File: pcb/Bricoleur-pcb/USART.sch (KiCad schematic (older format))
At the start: 1 part, among them J3 Conn_02x03_Odd_Even

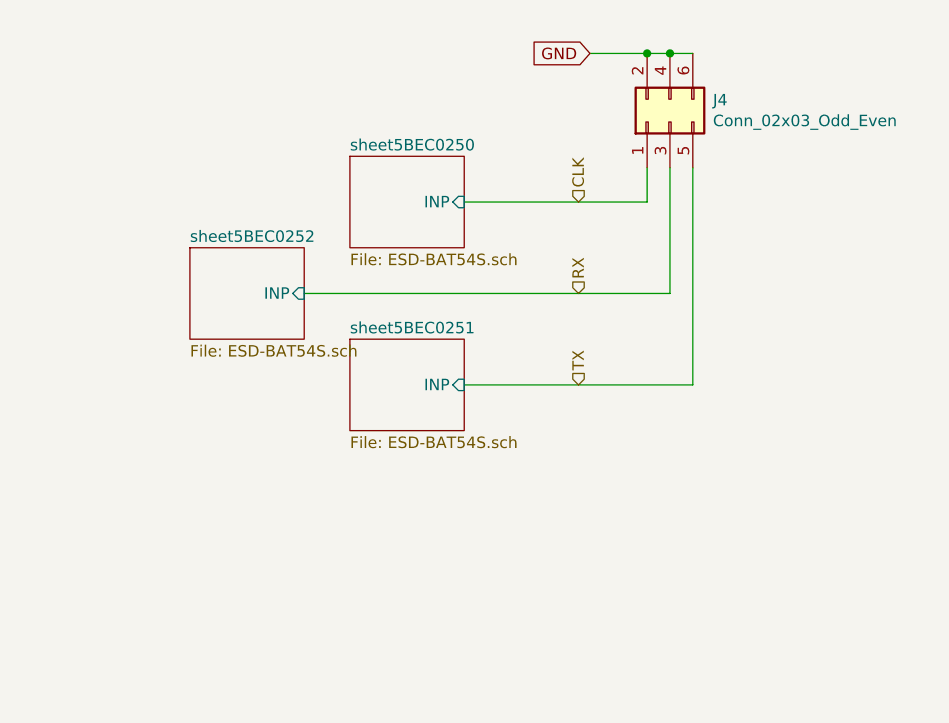
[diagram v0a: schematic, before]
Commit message: Narrowed down component placement, continued routing
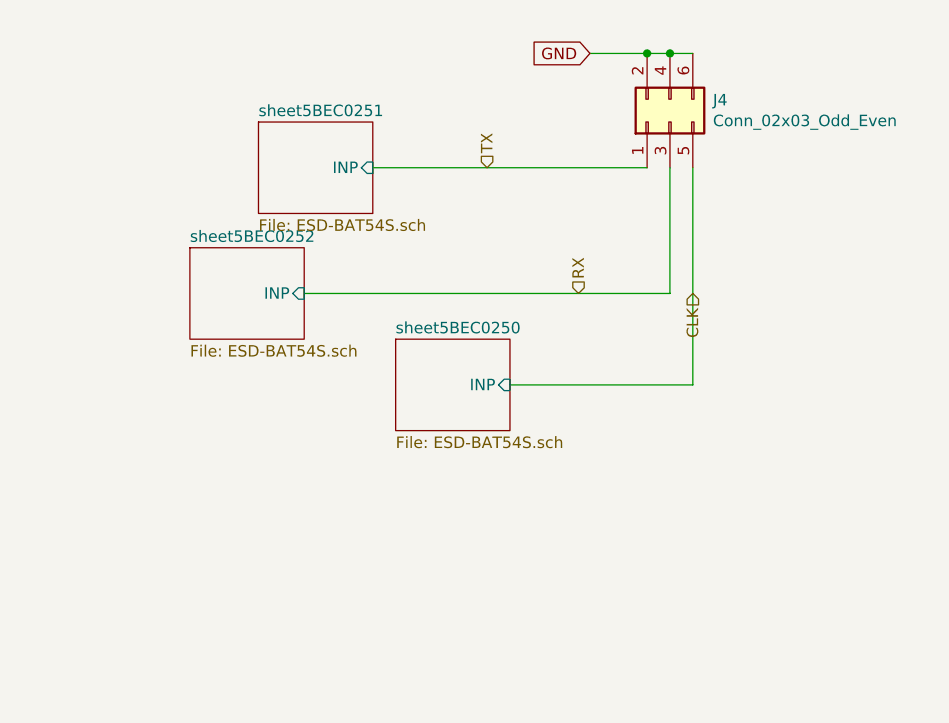
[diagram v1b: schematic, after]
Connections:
- net CLK: now also J3.5 (Pin_5); no longer J3.1 (Pin_1)
- net TX: now also J3.1 (Pin_1); no longer J3.5 (Pin_5)
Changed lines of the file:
@@
 $Descr A4 11693 8268
 encoding utf-8
-Sheet 11 18
+Sheet 15 18
 Title ""
 Date ""
@@
 $EndDescr
 $Sheet
-S 2300 2500 500  400
+S 2500 3300 500  400
 U 5BEC0255
 F0 "sheet5BEC0250" 50
 F1 "ESD-BAT54S.sch" 50
-F2 "INP" I R 2800 2700 50
+F2 "INP" I R 3000 3500 50
 $EndSheet
 $Sheet
-S 2300 3300 500  400
+S 1900 2350 500  400
 U 5BEC0258
 F0 "sheet5BEC0251" 50
 F1 "ESD-BAT54S.sch" 50
-F2 "INP" I R 2800 3500 50
+F2 "INP" I R 2400 2550 50
 $EndSheet
 $Sheet
@@
 $EndComp
 Wire Wire Line
-	3600 2550 3600 2700
-Wire Wire Line
-	2800 2700 3600 2700
+	3000 3500 3800 3500
 Wire Wire Line
 	3700 2550 3700 3100
@@
 Wire Wire Line
 	3800 2550 3800 3500
-Wire Wire Line
-	2800 3500 3800 3500
 Text GLabel 3350 2050 0    50   Input ~ 0
 GND
@@
 	3700 2050 3800 2050
 Connection ~ 3700 2050
-Text HLabel 3300 2700 1    50   Input ~ 0
+Text HLabel 3800 3100 3    50   Input ~ 0
 CLK
 Text HLabel 3300 3100 1    50   Input ~ 0
 RX
-Text HLabel 3300 3500 1    50   Input ~ 0
+Text HLabel 2900 2550 1    50   Input ~ 0
 TX
+Wire Wire Line
+	2400 2550 3600 2550
 $EndSCHEMATC

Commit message: Moar routing
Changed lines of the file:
@@
 $Descr A4 11693 8268
 encoding utf-8
-Sheet 15 18
+Sheet 11 18
 Title ""
 Date ""
@@
 AR Path="/5BEB800B/5BEC0490" Ref="J3"  Part="1"
 AR Path="/5BEE7FFD/5BEC0490" Ref="J4"  Part="1"
-F 0 "J4" V 3796 2162 50  0000 R CNN
+F 0 "J3" V 3796 2162 50  0000 R CNN
 F 1 "Conn_02x03_Odd_Even" V 3705 2162 50  0000 R CNN
 F 2 "Connector_IDC:IDC-Header_2x03_P2.54mm_Vertical" H 3700 2350 50  0001 C CNN

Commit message: Big fookup.
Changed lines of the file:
@@
 $Descr A4 11693 8268
 encoding utf-8
-Sheet 11 18
+Sheet 15 18
 Title ""
 Date ""
@@
 AR Path="/5BEB800B/5BEC0490" Ref="J3"  Part="1"
 AR Path="/5BEE7FFD/5BEC0490" Ref="J4"  Part="1"
-F 0 "J3" V 3796 2162 50  0000 R CNN
+F 0 "J4" V 3796 2162 50  0000 R CNN
 F 1 "Conn_02x03_Odd_Even" V 3705 2162 50  0000 R CNN
 F 2 "Connector_IDC:IDC-Header_2x03_P2.54mm_Vertical" H 3700 2350 50  0001 C CNN

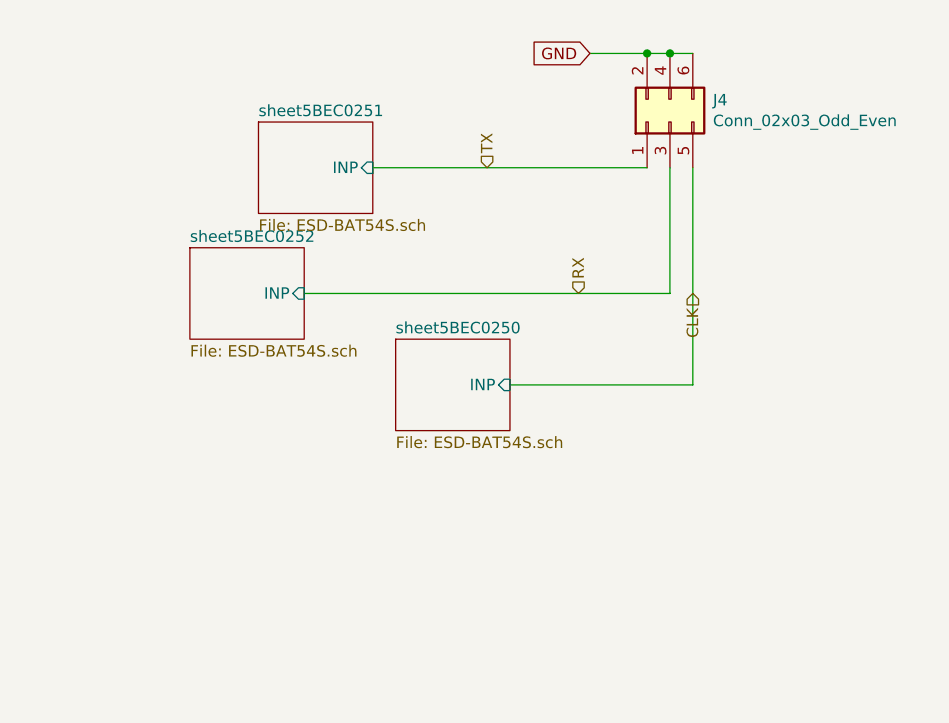
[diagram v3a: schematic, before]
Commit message: Cleanup, labeling, schematic size reduction
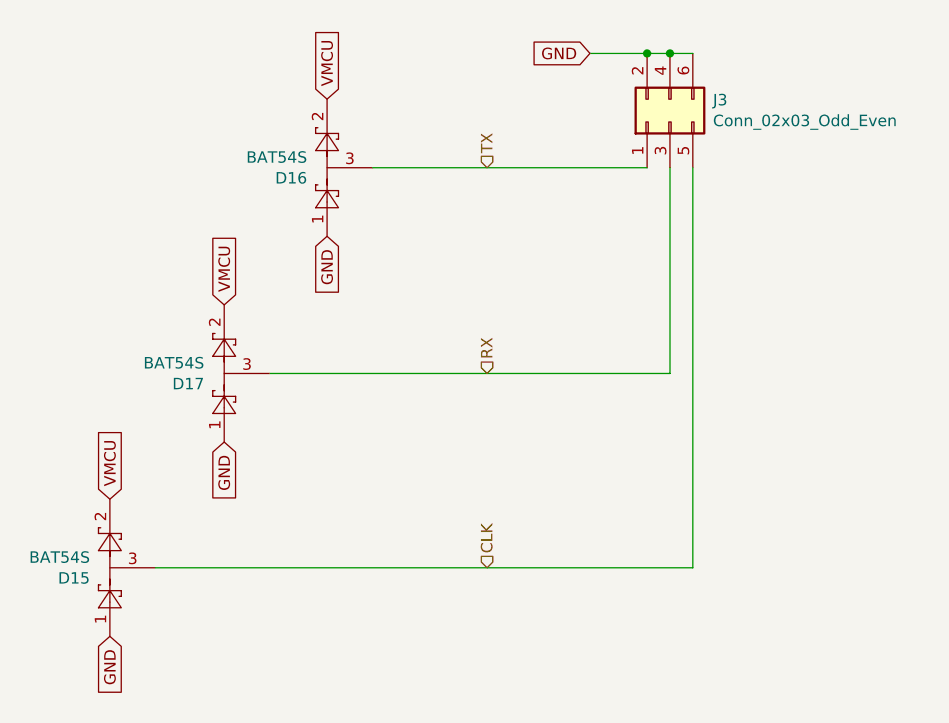
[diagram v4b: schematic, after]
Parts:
- added D17, D18, D19: BAT54S, Package_TO_SOT_SMD:SOT-23, symbol Diode:BAT54S
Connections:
- net CLK: now also D18.3
- net GND: now also D17.1, D18.1, D19.1
- net RX: now also D17.3
- net TX: now also D19.3
- new net VMCU: D17.2, D18.2, D19.2
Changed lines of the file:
@@
 $Descr A4 11693 8268
 encoding utf-8
-Sheet 15 18
+Sheet 4 5
 Title ""
 Date ""
@@
 Comment4 ""
 $EndDescr
-$Sheet
-S 2500 3300 500  400
-U 5BEC0255
-F0 "sheet5BEC0250" 50
-F1 "ESD-BAT54S.sch" 50
-F2 "INP" I R 3000 3500 50
-$EndSheet
-$Sheet
-S 1900 2350 500  400
-U 5BEC0258
-F0 "sheet5BEC0251" 50
-F1 "ESD-BAT54S.sch" 50
-F2 "INP" I R 2400 2550 50
-$EndSheet
-$Sheet
-S 1600 2900 500  400
-U 5BEC025B
-F0 "sheet5BEC0252" 50
-F1 "ESD-BAT54S.sch" 50
-F2 "INP" I R 2100 3100 50
-$EndSheet
 $Comp
 L Connector_Generic:Conn_02x03_Odd_Even J3
@@
 AR Path="/5BEB800B/5BEC0490" Ref="J3"  Part="1"
 AR Path="/5BEE7FFD/5BEC0490" Ref="J4"  Part="1"
-F 0 "J4" V 3796 2162 50  0000 R CNN
+F 0 "J3" V 3796 2162 50  0000 R CNN
 F 1 "Conn_02x03_Odd_Even" V 3705 2162 50  0000 R CNN
 F 2 "Connector_IDC:IDC-Header_2x03_P2.54mm_Vertical" H 3700 2350 50  0001 C CNN
@@
 $EndComp
 Wire Wire Line
-	3000 3500 3800 3500
+	1450 4300 3800 4300
 Wire Wire Line
-	3700 2550 3700 3100
+	3700 2550 3700 3450
 Wire Wire Line
-	2100 3100 3700 3100
+	1950 3450 3700 3450
 Wire Wire Line
-	3800 2550 3800 3500
+	3800 2550 3800 4300
 Text GLabel 3350 2050 0    50   Input ~ 0
 GND
@@
 	3700 2050 3800 2050
 Connection ~ 3700 2050
-Text HLabel 3800 3100 3    50   Input ~ 0
+Text HLabel 2900 4300 1    50   Input ~ 0
 CLK
-Text HLabel 3300 3100 1    50   Input ~ 0
+Text HLabel 2900 3450 1    50   Input ~ 0
 RX
 Text HLabel 2900 2550 1    50   Input ~ 0
@@
 Wire Wire Line
 	2400 2550 3600 2550
+$Comp
+L Diode:BAT54S D?
+U 1 1 5BFCE38E
+P 1250 4300
+AR Path="/5BB71F0F/5BFCE38E" Ref="D?"  Part="1"
+AR Path="/5BB7B6EA/5BFCE38E" Ref="D?"  Part="1"
+AR Path="/5BCBFDFB/5BFCE38E" Ref="D?"  Part="1"
+AR Path="/5BDAE386/5BDAE7CD/5BFCE38E" Ref="D?"  Part="1"
+AR Path="/5BDAE386/5BDAE90A/5BFCE38E" Ref="D?"  Part="1"
+AR Path="/5BDAE386/5BDAE977/5BFCE38E" Ref="D?"  Part="1"
+AR Path="/5BDAE386/5BDAEF7E/5BFCE38E" Ref="D?"  Part="1"
+AR Path="/5BEB800B/5BEC0255/5BFCE38E" Ref="D?"  Part="1"
+AR Path="/5BEB800B/5BEC0258/5BFCE38E" Ref="D?"  Part="1"
+AR Path="/5BEB800B/5BEC025B/5BFCE38E" Ref="D?"  Part="1"
+AR Path="/5BEE7FFD/5BEC0255/5BFCE38E" Ref="D?"  Part="1"
+AR Path="/5BEE7FFD/5BEC0258/5BFCE38E" Ref="D?"  Part="1"
+AR Path="/5BEE7FFD/5BEC025B/5BFCE38E" Ref="D?"  Part="1"
+AR Path="/5BEE7FFD/5BFCE38E" Ref="D18"  Part="1"
+AR Path="/5BEB800B/5BFCE38E" Ref="D15"  Part="1"
+F 0 "D15" V 1204 4387 50  0000 L CNN
+F 1 "BAT54S" V 1295 4387 50  0000 L CNN
+F 2 "Package_TO_SOT_SMD:SOT-23" H 1325 4425 50  0001 L CNN
+F 3 "https://www.diodes.com/assets/Datasheets/ds11005.pdf" H 1130 4300 50  0001 C CNN
+	1    1250 4300
+	0    -1   -1   0
+$EndComp
+Text GLabel 1250 4600 3    50   Input ~ 0
+GND
+Text GLabel 1250 4000 1    50   Input ~ 0
+VMCU
+$Comp
+L Diode:BAT54S D?
+U 1 1 5BFCE61A
+P 1750 3450
+AR Path="/5BB71F0F/5BFCE61A" Ref="D?"  Part="1"
+AR Path="/5BB7B6EA/5BFCE61A" Ref="D?"  Part="1"
+AR Path="/5BCBFDFB/5BFCE61A" Ref="D?"  Part="1"
+AR Path="/5BDAE386/5BDAE7CD/5BFCE61A" Ref="D?"  Part="1"
+AR Path="/5BDAE386/5BDAE90A/5BFCE61A" Ref="D?"  Part="1"
+AR Path="/5BDAE386/5BDAE977/5BFCE61A" Ref="D?"  Part="1"
+AR Path="/5BDAE386/5BDAEF7E/5BFCE61A" Ref="D?"  Part="1"
+AR Path="/5BEB800B/5BEC0255/5BFCE61A" Ref="D?"  Part="1"
+AR Path="/5BEB800B/5BEC0258/5BFCE61A" Ref="D?"  Part="1"
+AR Path="/5BEB800B/5BEC025B/5BFCE61A" Ref="D?"  Part="1"
+AR Path="/5BEE7FFD/5BEC0255/5BFCE61A" Ref="D?"  Part="1"
+AR Path="/5BEE7FFD/5BEC0258/5BFCE61A" Ref="D?"  Part="1"
+AR Path="/5BEE7FFD/5BEC025B/5BFCE61A" Ref="D?"  Part="1"
+AR Path="/5BEB800B/5BFCE61A" Ref="D17"  Part="1"
+AR Path="/5BEE7FFD/5BFCE61A" Ref="D20"  Part="1"
+F 0 "D17" V 1704 3537 50  0000 L CNN
+F 1 "BAT54S" V 1795 3537 50  0000 L CNN
+F 2 "Package_TO_SOT_SMD:SOT-23" H 1825 3575 50  0001 L CNN
+F 3 "https://www.diodes.com/assets/Datasheets/ds11005.pdf" H 1630 3450 50  0001 C CNN
+	1    1750 3450
+	0    -1   -1   0
+$EndComp
+Text GLabel 1750 3750 3    50   Input ~ 0
+GND
+Text GLabel 1750 3150 1    50   Input ~ 0
+VMCU
+$Comp
+L Diode:BAT54S D?
+U 1 1 5BFCE778
+P 2200 2550
+AR Path="/5BB71F0F/5BFCE778" Ref="D?"  Part="1"
+AR Path="/5BB7B6EA/5BFCE778" Ref="D?"  Part="1"
+AR Path="/5BCBFDFB/5BFCE778" Ref="D?"  Part="1"
+AR Path="/5BDAE386/5BDAE7CD/5BFCE778" Ref="D?"  Part="1"
+AR Path="/5BDAE386/5BDAE90A/5BFCE778" Ref="D?"  Part="1"
+AR Path="/5BDAE386/5BDAE977/5BFCE778" Ref="D?"  Part="1"
+AR Path="/5BDAE386/5BDAEF7E/5BFCE778" Ref="D?"  Part="1"
+AR Path="/5BEB800B/5BEC0255/5BFCE778" Ref="D?"  Part="1"
+AR Path="/5BEB800B/5BEC0258/5BFCE778" Ref="D?"  Part="1"
+AR Path="/5BEB800B/5BEC025B/5BFCE778" Ref="D?"  Part="1"
+AR Path="/5BEE7FFD/5BEC0255/5BFCE778" Ref="D?"  Part="1"
+AR Path="/5BEE7FFD/5BEC0258/5BFCE778" Ref="D?"  Part="1"
+AR Path="/5BEE7FFD/5BEC025B/5BFCE778" Ref="D?"  Part="1"
+AR Path="/5BEE7FFD/5BFCE778" Ref="D19"  Part="1"
+AR Path="/5BEB800B/5BFCE778" Ref="D16"  Part="1"
+F 0 "D16" V 2154 2637 50  0000 L CNN
+F 1 "BAT54S" V 2245 2637 50  0000 L CNN
+F 2 "Package_TO_SOT_SMD:SOT-23" H 2275 2675 50  0001 L CNN
+F 3 "https://www.diodes.com/assets/Datasheets/ds11005.pdf" H 2080 2550 50  0001 C CNN
+	1    2200 2550
+	0    -1   -1   0
+$EndComp
+Text GLabel 2200 2850 3    50   Input ~ 0
+GND
+Text GLabel 2200 2250 1    50   Input ~ 0
+VMCU
 $EndSCHEMATC
